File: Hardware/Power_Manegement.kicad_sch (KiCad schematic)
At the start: 3 parts, among them U12 USB4105

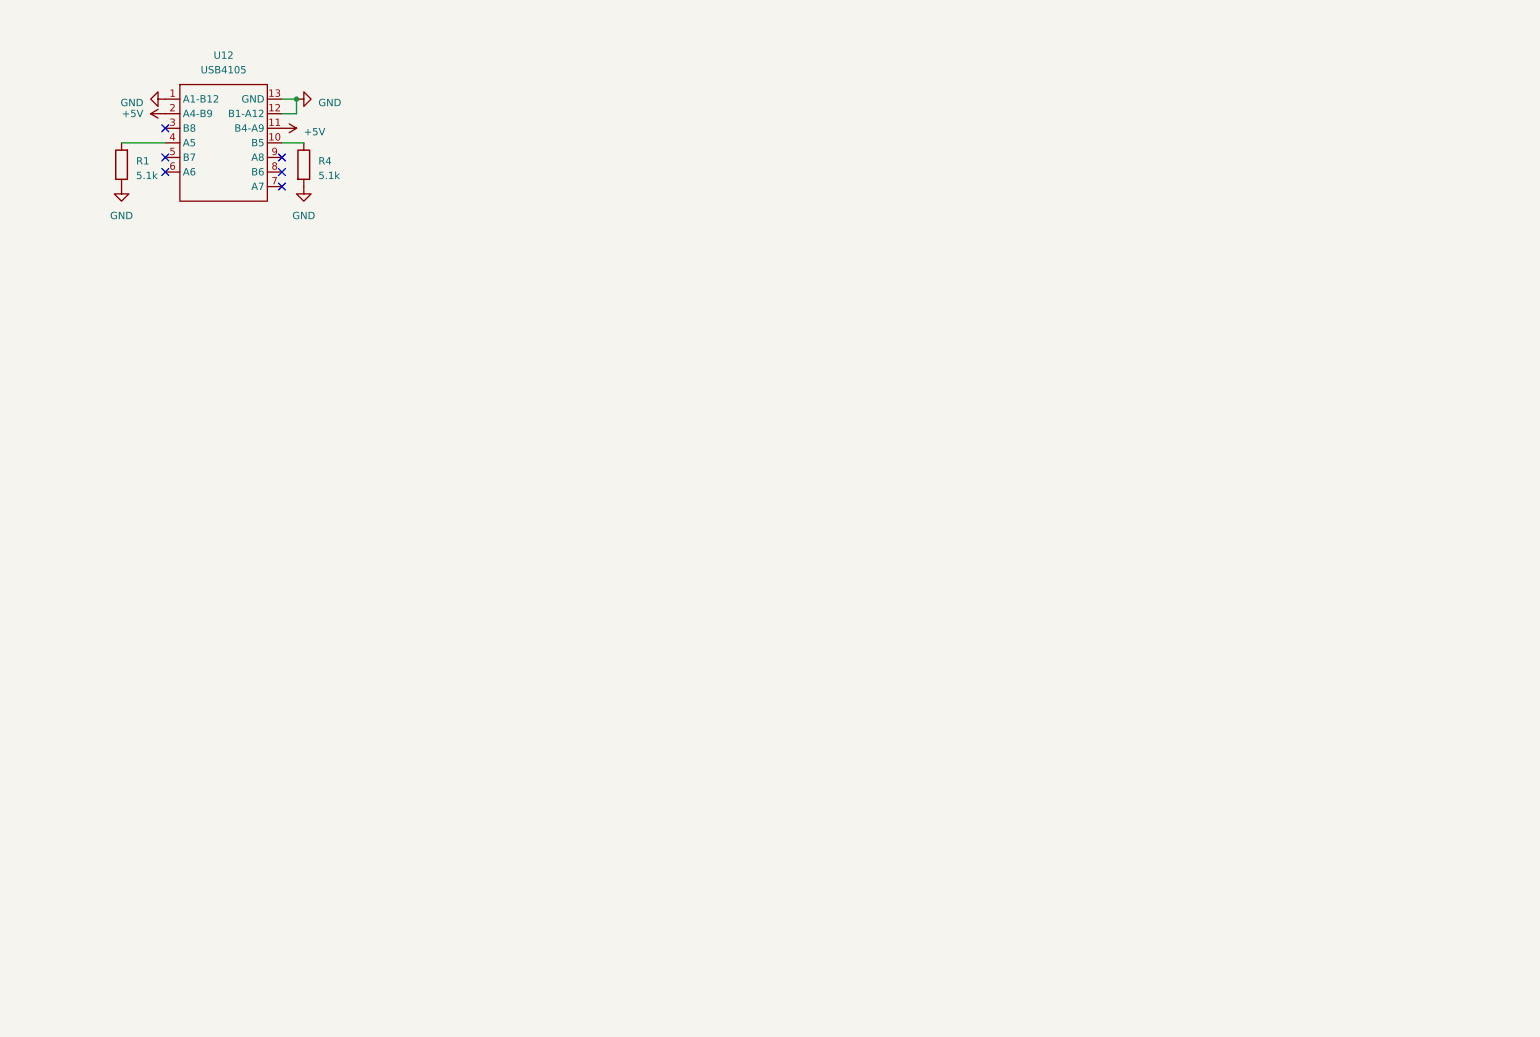
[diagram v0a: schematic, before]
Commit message: Add charging circuitry
Warning Voltage dividers for switching regulator not speced correctly!!
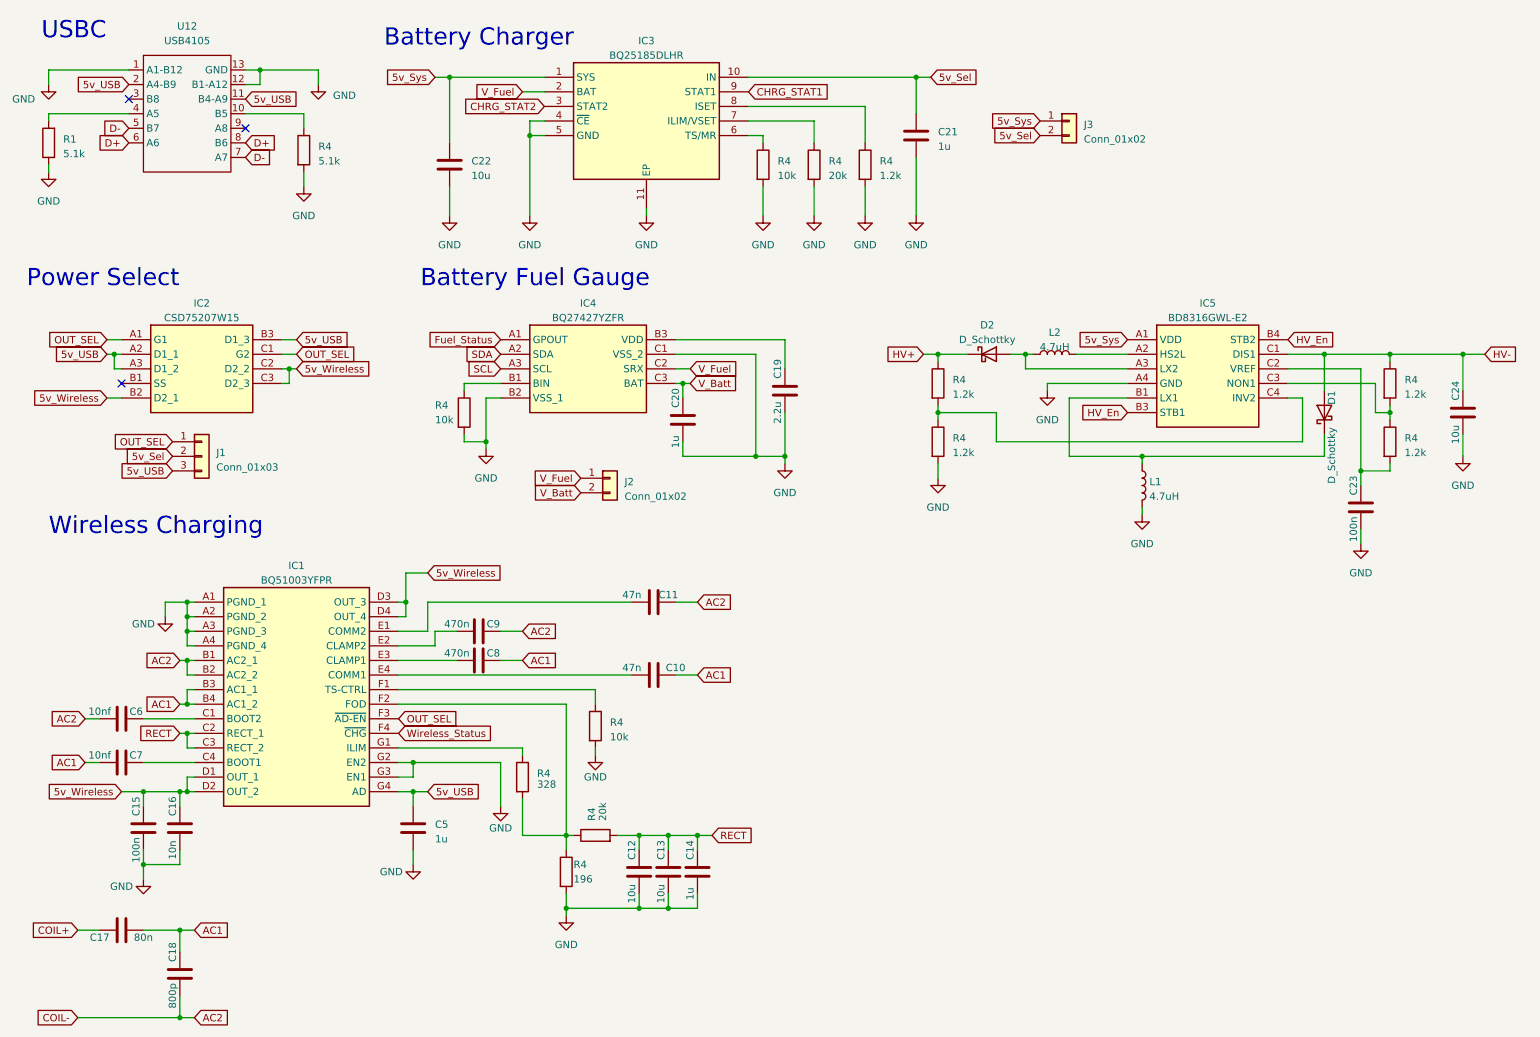
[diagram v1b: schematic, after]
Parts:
- added C10, C11: 47n, symbol Device:C
- added C12, C13, C22, C24: 10u, symbol Device:C
- added C14, C20, C21, C5: 1u, symbol Device:C
- added C15, C23: 100n, symbol Device:C
- added C16: 10n, symbol Device:C
- added C17: 80n, symbol Device:C
- added C18: 800p, symbol Device:C
- added C19: 2.2u, symbol Device:C
- added C6, C7: 10nf, symbol Device:C
- added C8, C9: 470n, symbol Device:C
- added D1, D2: D_Schottky, symbol Device:D_Schottky
- added IC1: BQ51003YFPR, BQ51003YFPR:BGA28C40P4X7_188X301X50, symbol BQ51003YFPR:BQ51003YFPR
- added IC2: CSD75207W15, BQ51003YFPR:BGA9C50P3X3_146X146X62, symbol CSD75207W15:CSD75207W15
- added IC3: BQ25185DLHR, BQ51003YFPR:SON40P220X200X80-11N, symbol BQ25185DLHR:BQ25185DLHR
- added IC4: BQ27427YZFR, BQ51003YFPR:BGA9C50P3X3_158X162X62, symbol BQ27427YZFR:BQ27427YZFR
- added IC5: BD8316GWL-E2, BQ51003YFPR:BGA11C40P4X3_180X150X55, symbol BD8316GWL-E2:BD8316GWL-E2
- added J1: Conn_01x03, symbol Connector_Generic:Conn_01x03
- added J2, J3: Conn_01x02, symbol Connector_Generic:Conn_01x02
- added L1, L2: 4.7uH, symbol Device:L
- added R4 (x2): 20k, Resistor_SMD:R_0805_2012Metric, symbol Device:R
- added R4 (x3): 10k, Resistor_SMD:R_0805_2012Metric, symbol Device:R
- added R4 (x5): 1.2k, Resistor_SMD:R_0805_2012Metric, symbol Device:R
- added R4: 196, Resistor_SMD:R_0805_2012Metric, symbol Device:R
- added R4: 328, Resistor_SMD:R_0805_2012Metric, symbol Device:R
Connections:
- net GND: now also C12.2, C13.2, C14.2, C15.2, C16.2, C19.2, C20.2, C21.2, C22.2, C23.2, C24.2, C5.2, IC1.A1 (PGND_1), IC1.A2 (PGND_2), IC1.A3 (PGND_3), IC1.A4 (PGND_4), IC1.G2 (EN2), IC1.G3 (EN1), IC3.11 (EP), IC3.4 (~{CE}), IC3.5 (GND), IC4.B2 (VSS_1), IC4.C1 (VSS_2), IC5.A4 (GND), L1.2, R4.2, R4.2, R4.2, R4.2, R4.2, R4.2, R4.2
- net D-: now reaches U12.5 (B7)
- net D-: now also U12.7 (A7)
- net D+: now reaches U12.6 (A6)
- net D+: now also U12.8 (B6)
- net +5V renamed 5v_USB
- net 5v_USB: now also C5.1, IC1.G4 (AD), IC2.A2 (D1_1), IC2.A3 (D1_2), IC2.B3 (D1_3), J1.3 (Pin_3)
- new net: C23.1, IC5.C2 (VREF), R4.2
- new net: C6.1, IC1.C1 (BOOT2)
- new net: IC1.F2 (FOD), R4.1, R4.1, R4.2
- new net: IC3.6 (TS/MR), R4.1
- new net: C8.2, IC1.E3 (CLAMP1)
- new net: D1.1 (K), IC5.B1 (LX1), L1.1
- new net: IC5.A2 (HS2L), L2.2
- new net: D2.2 (A), IC5.A3 (LX2), L2.1
- new net: IC5.C3 (NON1), R4.1, R4.2
- new net: IC5.C4 (INV2), R4.1, R4.2
- new net: IC1.F1 (TS-CTRL), R4.1
- new net: IC3.7 (ILIM/VSET), R4.1
- new net: IC3.8 (ISET), R4.1
- new net: C7.1, IC1.C4 (BOOT1)
- new net: C11.2, IC1.E1 (COMM2)
- new net: C9.2, IC1.E2 (CLAMP2)
- new net: C10.2, IC1.E4 (COMM1)
- new net: IC1.G1 (ILIM), R4.1
- new net: IC4.B1 (BIN), R4.1
- new net: C19.1, IC4.B3 (VDD)
- new net 5v_Sel: C21.1, IC3.10 (IN), J1.2 (Pin_2), J3.2 (Pin_2)
- new net 5v_Sys: C22.1, IC3.1 (SYS), IC5.A1 (VDD), J3.1 (Pin_1)
- new net 5v_Wireless: C15.1, C16.1, IC1.D1 (OUT_1), IC1.D2 (OUT_2), IC1.D3 (OUT_3), IC1.D4 (OUT_4), IC2.B2 (D2_1), IC2.C2 (D2_2), IC2.C3 (D2_3)
- new net AC1: C10.1, C17.2, C18.1, C7.2, C8.1, IC1.B3 (AC1_1), IC1.B4 (AC1_2)
- new net AC2: C11.1, C18.2, C6.2, C9.1, IC1.B1 (AC2_1), IC1.B2 (AC2_2)
- new net CHRG_STAT1: IC3.9 (STAT1)
- new net CHRG_STAT2: IC3.3 (STAT2)
- new net COIL+: C17.1
- new net Fuel_Status: IC4.A1 (GPOUT)
- new net HV+: D2.1 (K), R4.1
- new net HV-: C24.1, D1.2 (A), IC5.C1 (DIS1), R4.1
- new net HV_En: IC5.B3 (STB1), IC5.B4 (STB2)
- new net OUT_SEL: IC1.F3 (~{AD-EN}), IC2.A1 (G1), IC2.C1 (G2), J1.1 (Pin_1)
- new net RECT: C12.1, C13.1, C14.1, IC1.C2 (RECT_1), IC1.C3 (RECT_2), R4.2
- new net SCL: IC4.A3 (SCL)
- new net SDA: IC4.A2 (SDA)
- new net V_Batt: C20.1, IC4.C3 (BAT), J2.2 (Pin_2)
- new net V_Fuel: IC3.2 (BAT), IC4.C2 (SRX), J2.1 (Pin_1)
- new net Wireless_Status: IC1.F4 (~{CHG})
- no-connect marks 6 -> 3
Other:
- note added: "Battery Charger"
- note added: "Battery Fuel Gauge"
- note added: "Power Select"
- note added: "USBC"
- note added: "Wireless Charging"
- moved on the sheet: R1, R4, U12

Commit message: Power Management Complete
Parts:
- removed J3: Conn_01x02, symbol Connector_Generic:Conn_01x02
- added C25, C26, C27, C28, C29, C30, C33, C34: 10u, symbol Device:C
- added C31, C32: 10n, symbol Device:C
- added IC6: TLV62585DRLR, BQ51003YFPR:SOTFL50P160X60-6N, symbol TLV62585DRLR:TLV62585DRLR
- added IC7: TPS7A3901DSCR, BQ51003YFPR:SON50P300X300X80-11N-D, symbol TPS7A3901DSCR:TPS7A3901DSCR
- added J10, J11, J3: Conn_01x03, symbol Connector_Generic:Conn_01x03
- added J4, J5, J6, J7, J8: Conn_01x02, symbol Connector_Generic:Conn_01x02
- added J9: S2B-PH-SM4-TB, BQ51003YFPR:CONN_S2B-PH-SM4-TB_JST, symbol 2024-03-26_04-39-57:S2B-PH-SM4-TB
- added L3: 1uH, symbol Device:L
- added R4: 100k, Resistor_SMD:R_0805_2012Metric, symbol Device:R
- added R4 (x2): 10k, Resistor_SMD:R_0805_2012Metric, symbol Device:R
- added R4: 28k, Resistor_SMD:R_0805_2012Metric, symbol Device:R
- added R4: 17.8k, Resistor_SMD:R_0805_2012Metric, symbol Device:R
- added R4: 450k, Resistor_SMD:R_0805_2012Metric, symbol Device:R
- R4: value 1.2k -> 102.5k
- R4: value 1.2k -> 3k
- R4: value 1.2k -> 10k
- R4: value 20k -> 130k
- R4: value 1.2k -> 90k
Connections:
- net 5v_Sel: now also J3.3 (Pin_3)
- net 5v_Sys: now also C26.1, C27.1, IC6.3 (VIN), IC6.4 (EN), J3.2 (Pin_2); no longer C22.1, IC3.1 (SYS)
- net GND: now also C25.2, C26.2, C27.2, C28.2, C29.2, C30.2, IC6.1 (GND), IC7.4 (GND), J10.3 (Pin_3), J11.3 (Pin_3), J9.3 (SHIELD), J9.4 (SHIELD), R4.2
- net V_Batt: now also J10.1 (Pin_1), J11.1 (Pin_1)
- net HV+ renamed +9v
- net +9v: now also C25.1, C30.1, IC7.1 (INP), IC7.2 (EN), J5.1 (Pin_1)
- net HV- renamed -9v
- net -9v: now also C29.1, IC7.5 (INN), J6.1 (Pin_1)
- new net: IC6.5 (FB), R4.1, R4.2
- new net: C31.1, IC7.7 (FBN), R4.1, R4.2
- new net: IC7.8 (BUF), R4.1
- new net: C32.2, C34.1, IC7.9 (FBP), R4.1, R4.2
- new net: IC6.2 (SW), L3.2
- new net +3.3V: J4.1 (Pin_1)
- new net +3.3VA: J7.1 (Pin_1)
- new net +3.3va: C32.1, IC7.10 (OUTP), J7.2 (Pin_2), R4.1
- new net +3v: C28.1, J4.2 (Pin_2), L3.1, R4.1
- new net -3.3va: C31.2, C33.1, IC7.6 (OUTN), J8.2 (Pin_2), R4.2
- new net -3V3: J8.1 (Pin_1)
- new net 5v_Batt: C22.1, IC3.1 (SYS), J3.1 (Pin_1)
- new net Batt+: J10.2 (Pin_2), J9.1
- new net Batt-: J11.2 (Pin_2), J9.2
- new net GNDA: C33.2, C34.2, IC7.11 (EP), R4.2
- new net Stim+: J5.2 (Pin_2)
- new net Stim-: J6.2 (Pin_2)
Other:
- note added: "Analog Power Supply"
- note added: "Battery"
- note added: "PRT-13851 Battery - 400mAh - 400mA max - 3.7v nom - 4.2V max - 2.8v discharge"
- note added: "Stim Power Supply"
- note added: "System Power Supply"
- moved on the sheet: C10, C11, C12, C13, C14, C15, C16, C17, C18, C19, C20, C21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

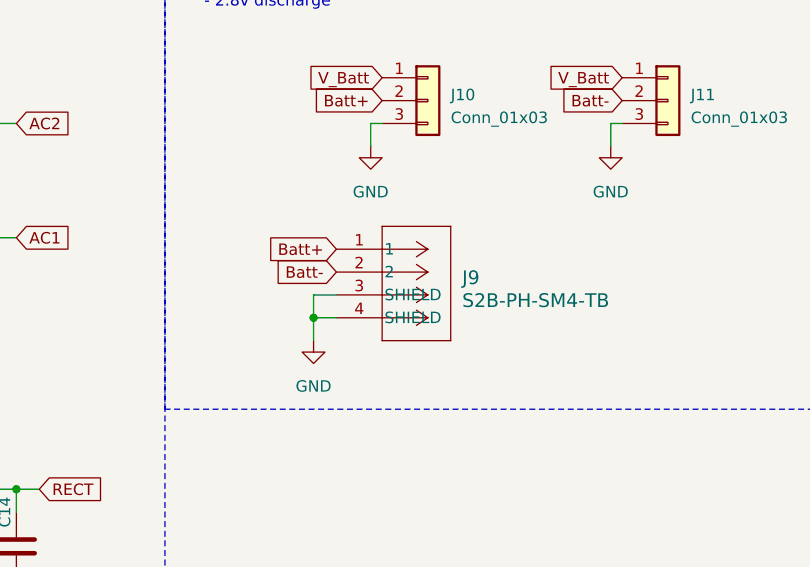
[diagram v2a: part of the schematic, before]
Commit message: Design Analog Frontend
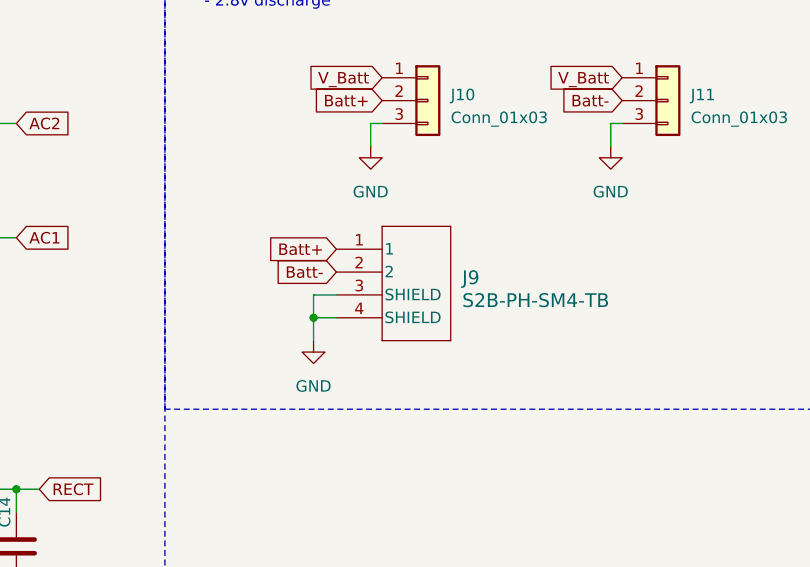
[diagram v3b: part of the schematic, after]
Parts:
- R1, R4: footprint Resistor_SMD:R_0805_2012Metric -> (none)
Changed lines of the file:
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@@
       (effects (font (size 1.27 1.27)) (justify left))
     )
-    (property "Footprint" "Resistor_SMD:R_0805_2012Metric" (at 272.542 201.93 90)
+    (property "Footprint" "" (at 272.542 201.93 90)
       (effects (font (size 1.27 1.27)) hide)
     )
@@
       (effects (font (size 1.27 1.27)) (justify left))
     )
-    (property "Footprint" "Resistor_SMD:R_0805_2012Metric" (at 134.62 230.378 90)
+    (property "Footprint" "" (at 134.62 230.378 90)
       (effects (font (size 1.27 1.27)) hide)
     )
@@
       (effects (font (size 1.27 1.27)) (justify left))
     )
-    (property "Footprint" "Resistor_SMD:R_0805_2012Metric" (at 183.642 55.88 90)
+    (property "Footprint" "" (at 183.642 55.88 90)
       (effects (font (size 1.27 1.27)) hide)
     )
@@
       (effects (font (size 1.27 1.27)) (justify left))
     )
-    (property "Footprint" "Resistor_SMD:R_0805_2012Metric" (at 132.842 209.55 90)
+    (property "Footprint" "" (at 132.842 209.55 90)
       (effects (font (size 1.27 1.27)) hide)
     )
@@
       (effects (font (size 1.27 1.27)) (justify left))
     )
-    (property "Footprint" "Resistor_SMD:R_0805_2012Metric" (at 280.162 124.46 90)
+    (property "Footprint" "" (at 280.162 124.46 90)
       (effects (font (size 1.27 1.27)) hide)
     )
@@
       (effects (font (size 1.27 1.27)) (justify left))
     )
-    (property "Footprint" "Resistor_SMD:R_0805_2012Metric" (at 127.762 234.95 90)
+    (property "Footprint" "" (at 127.762 234.95 90)
       (effects (font (size 1.27 1.27)) hide)
     )
@@
       (effects (font (size 1.27 1.27)) (justify left))
     )
-    (property "Footprint" "Resistor_SMD:R_0805_2012Metric" (at 201.422 55.88 90)
+    (property "Footprint" "" (at 201.422 55.88 90)
       (effects (font (size 1.27 1.27)) hide)
     )
@@
       (effects (font (size 1.27 1.27)) (justify left))
     )
-    (property "Footprint" "Resistor_SMD:R_0805_2012Metric" (at 280.162 134.62 90)
+    (property "Footprint" "" (at 280.162 134.62 90)
       (effects (font (size 1.27 1.27)) hide)
     )
@@
       (effects (font (size 1.27 1.27)) (justify right))
     )
-    (property "Footprint" "Resistor_SMD:R_0805_2012Metric" (at 41.148 55.88 90)
+    (property "Footprint" "" (at 41.148 55.88 90)
       (effects (font (size 1.27 1.27)) hide)
     )
@@
       (effects (font (size 1.27 1.27)) (justify left))
     )
-    (property "Footprint" "Resistor_SMD:R_0805_2012Metric" (at 120.142 218.44 90)
+    (property "Footprint" "" (at 120.142 218.44 90)
       (effects (font (size 1.27 1.27)) hide)
     )
@@
       (effects (font (size 1.27 1.27)) (justify left))
     )
-    (property "Footprint" "Resistor_SMD:R_0805_2012Metric" (at 324.612 55.88 90)
+    (property "Footprint" "" (at 324.612 55.88 90)
       (effects (font (size 1.27 1.27)) hide)
     )
@@
       (effects (font (size 1.27 1.27)) (justify left))
     )
-    (property "Footprint" "Resistor_SMD:R_0805_2012Metric" (at 358.902 134.62 90)
+    (property "Footprint" "" (at 358.902 134.62 90)
       (effects (font (size 1.27 1.27)) hide)
     )
@@
       (effects (font (size 1.27 1.27)) (justify left))
     )
-    (property "Footprint" "Resistor_SMD:R_0805_2012Metric" (at 192.532 55.88 90)
+    (property "Footprint" "" (at 192.532 55.88 90)
       (effects (font (size 1.27 1.27)) hide)
     )
@@
       (effects (font (size 1.27 1.27)) (justify left))
     )
-    (property "Footprint" "Resistor_SMD:R_0805_2012Metric" (at 342.392 55.88 90)
+    (property "Footprint" "" (at 342.392 55.88 90)
       (effects (font (size 1.27 1.27)) hide)
     )
@@
       (effects (font (size 1.27 1.27)) (justify left))
     )
-    (property "Footprint" "Resistor_SMD:R_0805_2012Metric" (at 156.972 133.35 90)
+    (property "Footprint" "" (at 156.972 133.35 90)
       (effects (font (size 1.27 1.27)) hide)
     )
@@
       (effects (font (size 1.27 1.27)) (justify left))
     )
-    (property "Footprint" "Resistor_SMD:R_0805_2012Metric" (at 324.612 66.04 90)
+    (property "Footprint" "" (at 324.612 66.04 90)
       (effects (font (size 1.27 1.27)) hide)
     )
@@
       (effects (font (size 1.27 1.27)) (justify left))
     )
-    (property "Footprint" "Resistor_SMD:R_0805_2012Metric" (at 342.392 43.18 90)
+    (property "Footprint" "" (at 342.392 43.18 90)
       (effects (font (size 1.27 1.27)) hide)
     )
@@
       (effects (font (size 1.27 1.27)) (justify left))
     )
-    (property "Footprint" "Resistor_SMD:R_0805_2012Metric" (at 82.042 57.15 90)
+    (property "Footprint" "" (at 82.042 57.15 90)
       (effects (font (size 1.27 1.27)) hide)
     )
@@
       (effects (font (size 1.27 1.27)) (justify left))
     )
-    (property "Footprint" "Resistor_SMD:R_0805_2012Metric" (at 358.902 124.46 90)
+    (property "Footprint" "" (at 358.902 124.46 90)
       (effects (font (size 1.27 1.27)) hide)
     )
@@
       (effects (font (size 1.27 1.27)) (justify left))
     )
-    (property "Footprint" "Resistor_SMD:R_0805_2012Metric" (at 272.542 191.77 90)
+    (property "Footprint" "" (at 272.542 191.77 90)
       (effects (font (size 1.27 1.27)) hide)
     )
